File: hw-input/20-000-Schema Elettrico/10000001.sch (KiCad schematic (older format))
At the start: 34 parts, among them P1 PLUG_01X04_254, P2 PLUG_01X04_254, P3 PLUG_01X04_254, P4 PLUG_01X04_254, P5 PLUG_01X04_254, P6 PLUG_01X04_254, P7 PLUG_01X04_254, P8 PLUG_01X04_254, U1 TCA9554, U2 TLP291(SE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

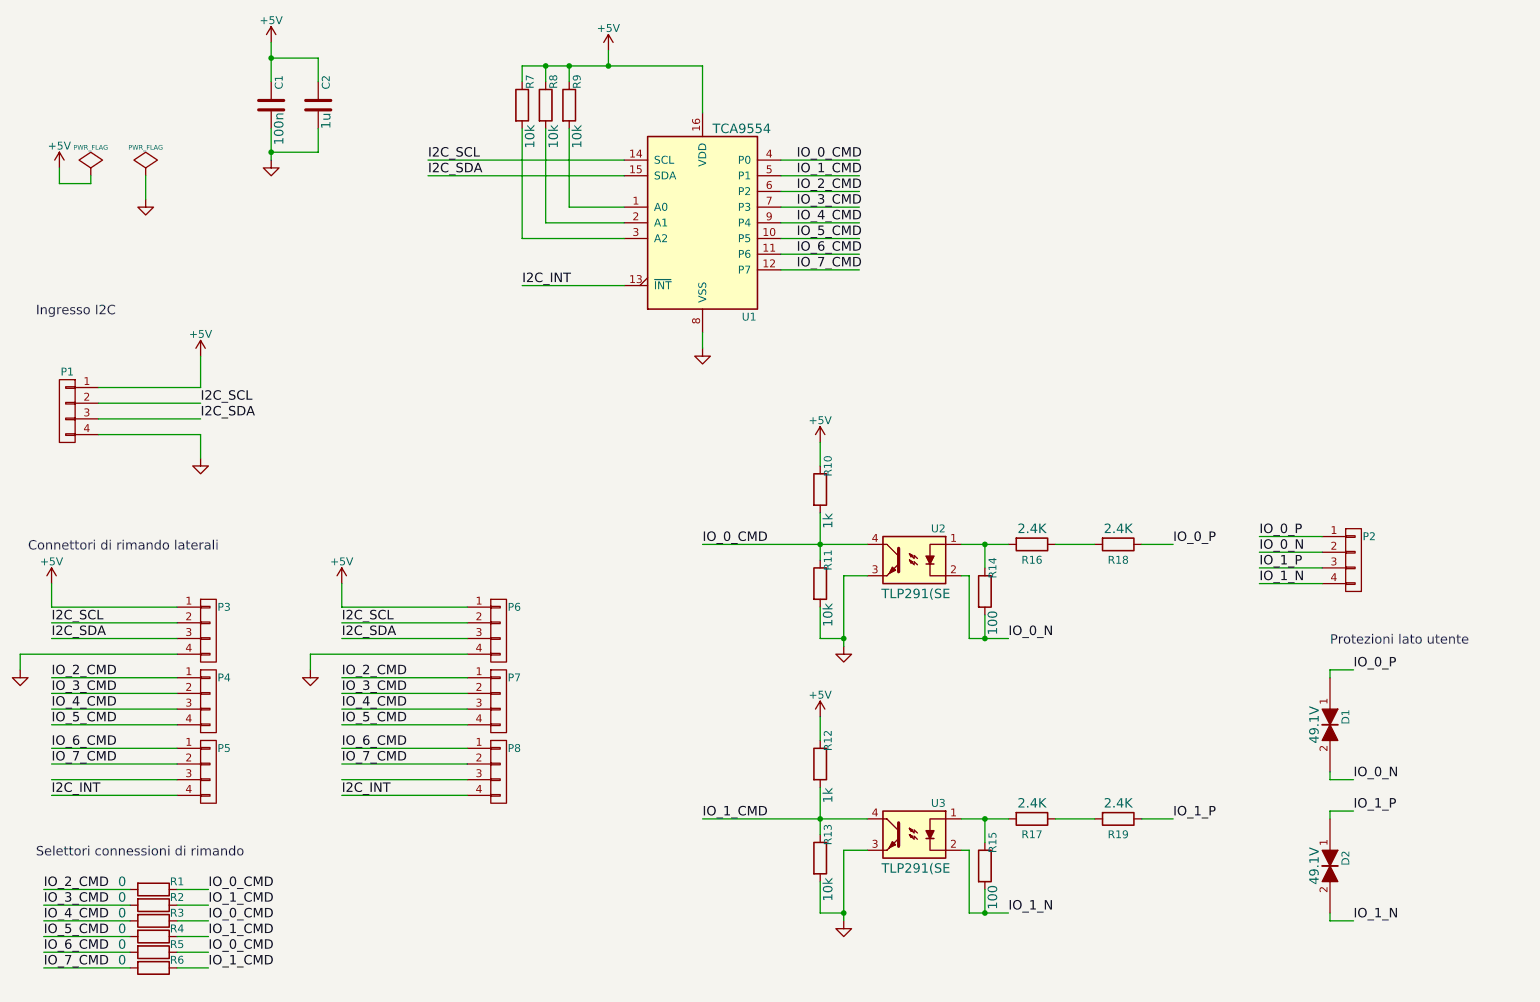
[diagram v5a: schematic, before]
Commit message: completato schema elettrico e sbroglio
Signed-off-by: CrazyDiamond <crazyd14@gmail.com>
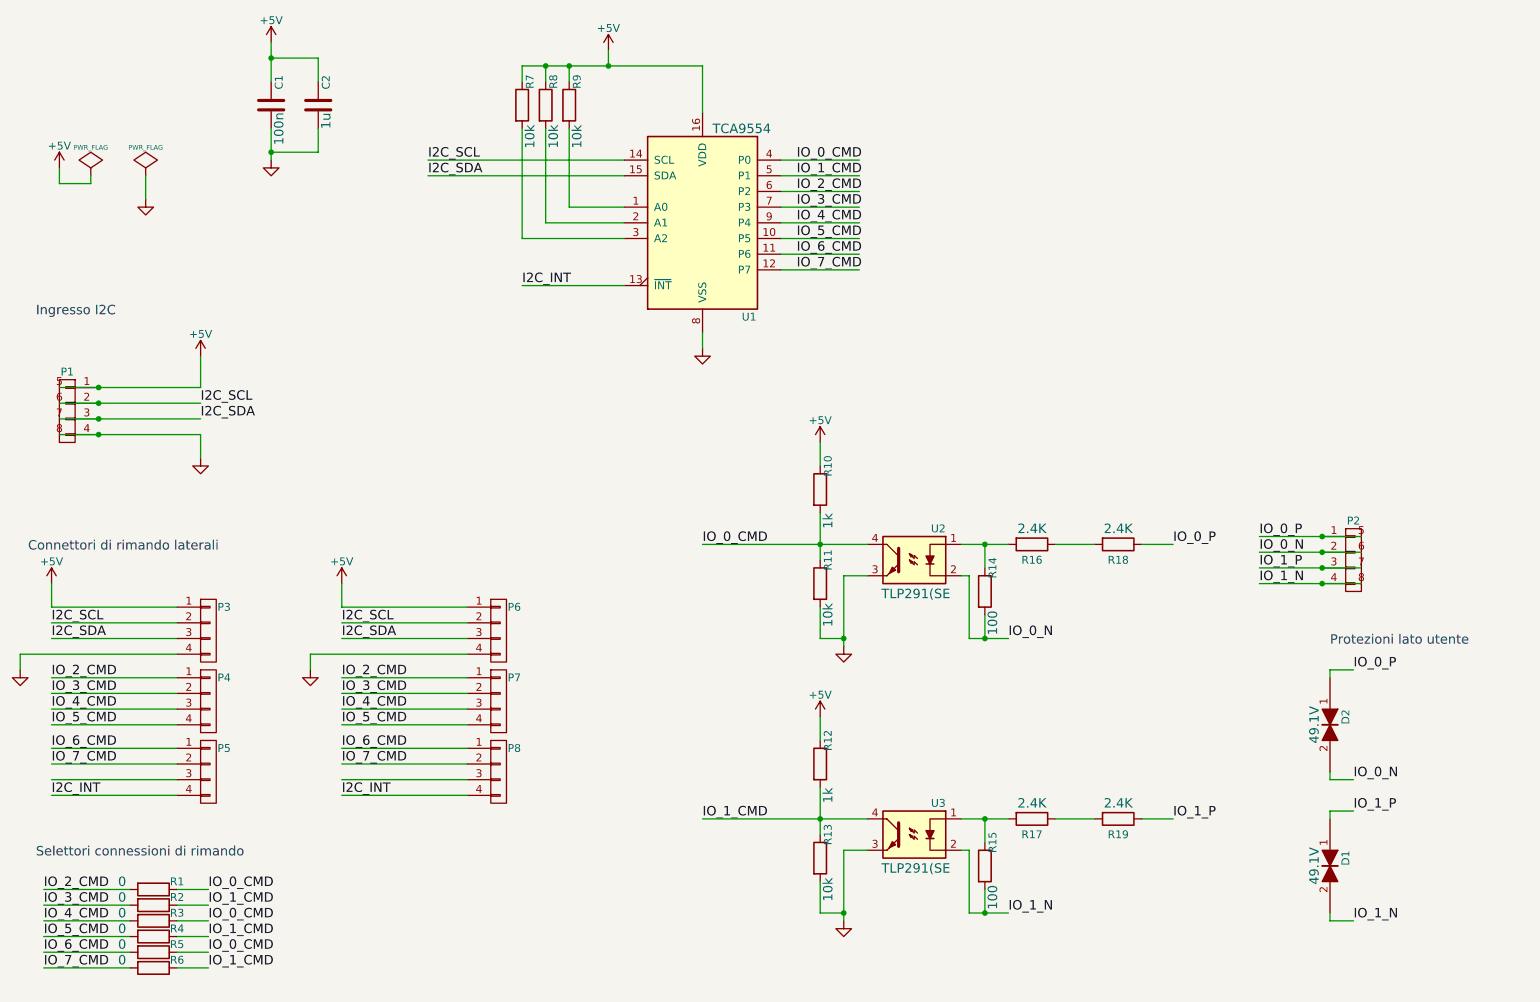
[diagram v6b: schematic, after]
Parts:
- removed P1, P2: PLUG_01X04_254, Socket_Strips:Socket_Strip_Straight_1x04, symbol PLUG_01X04_254
- added P1, P2: TERMINAL_01X04_250_RA_SPRING, os_terminal_block:1770908, symbol TERMINAL_01X04_250_RA_SPRING
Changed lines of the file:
@@
 	1550 1700 1550 1600
 Wire Wire Line
-	1800 3000 2450 3000
+	1550 3000 2450 3000
 Wire Wire Line
 	2450 3000 2450 2800
 Wire Wire Line
-	1800 3300 2450 3300
-Wire Wire Line
-	1800 3100 2450 3100
-Wire Wire Line
-	9600 3950 9200 3950
-Wire Wire Line
-	9600 4050 9200 4050
-Wire Wire Line
-	9600 4150 9200 4150
-Wire Wire Line
-	9600 4250 9200 4250
-Wire Wire Line
-	1800 3200 2450 3200
+	1550 3300 2450 3300
+Wire Wire Line
+	1550 3100 2450 3100
+Wire Wire Line
+	9200 3950 9850 3950
+Wire Wire Line
+	9200 4050 9850 4050
+Wire Wire Line
+	9200 4150 9850 4150
+Wire Wire Line
+	9200 4250 9850 4250
+Wire Wire Line
+	1550 3200 2450 3200
 Wire Wire Line
 	2450 3300 2450 3450
@@
 $EndComp
 $Comp
-L PLUG_01X04_254 P1
-U 1 1 56E8991D
-P 1600 3150
-F 0 "P1" H 1600 3400 50  0000 C CNN
-F 1 "PLUG_01X04_254" H 1700 3150 50  0001 C CNN
-F 2 "Socket_Strips:Socket_Strip_Straight_1x04" H 1500 3300 50  0001 C CNN
-F 3 "" H 1600 3400 50  0000 C CNN
-F 4 "0" H 1700 3500 60  0001 C CNN "NOPOP"
-F 5 "Harwin" H 1800 3600 60  0001 C CNN "MF"
-F 6 "M20-7820446" H 1900 3700 60  0001 C CNN "MF_PN"
-F 7 "M20-7820446" H 2000 3800 60  0001 C CNN "VAL"
-	1    1600 3150
-	-1   0    0    -1
-$EndComp
-$Comp
 L PLUG_01X04_254 P3
 U 1 1 56E89F8C
@@
 $EndComp
 $Comp
-L PLUG_01X04_254 P2
-U 1 1 56E8BD81
-P 9800 4100
-F 0 "P2" H 9900 4250 50  0000 C CNN
-F 1 "PLUG_01X04_254" H 9900 4100 50  0001 C CNN
-F 2 "Socket_Strips:Socket_Strip_Straight_1x04" H 9700 4250 50  0001 C CNN
-F 3 "" H 9800 4350 50  0000 C CNN
-F 4 "0" H 9900 4450 60  0001 C CNN "NOPOP"
-F 5 "Harwin" H 10000 4550 60  0001 C CNN "MF"
-F 6 "M20-7820446" H 10100 4650 60  0001 C CNN "MF_PN"
-F 7 "M20-7820446" H 10200 4750 60  0001 C CNN "VAL"
-	1    9800 4100
-	1    0    0    -1
-$EndComp
-$Comp
 L R_0_0603_5 R1
 U 1 1 56E8C920
@@
 U 1 1 56E8F00D
 P 9650 5150
-F 0 "D1" H 9600 5250 50  0000 C CNN
+F 0 "D2" H 9600 5250 50  0000 C CNN
 F 1 "TVS_SMC_49.1V" H 9650 5000 50  0001 C CNN
 F 2 "Diodes_SMD:SMC_Standard" H 9550 5200 50  0001 C CNN
@@
 U 1 1 56E8F0C7
 P 9650 6050
-F 0 "D2" H 9600 6150 50  0000 C CNN
+F 0 "D1" H 9600 6150 50  0000 C CNN
 F 1 "TVS_SMC_49.1V" H 9650 5900 50  0001 C CNN
 F 2 "Diodes_SMD:SMC_Standard" H 9550 6100 50  0001 C CNN
@@
 	1    0    0    -1
 $EndComp
+$Comp
+L TERMINAL_01X04_250_RA_SPRING P1
+U 1 1 57E1C341
+P 1600 3150
+F 0 "P1" H 1600 3400 50  0000 C CNN
+F 1 "TERMINAL_01X04_250_RA_SPRING" H 1700 3150 50  0001 C CNN
+F 2 "os_terminal_block:1770908" H 1500 3300 50  0001 C CNN
+F 3 "" H 1600 3400 50  0001 C CNN
+F 4 "0" H 1700 3500 60  0001 C CNN "NOPOP"
+F 5 "Phoenix Contact" H 1800 3600 60  0001 C CNN "MF"
+F 6 "1770908" H 1900 3700 60  0001 C CNN "MF_PN"
+F 7 "1770908" H 2000 3800 60  0001 C CNN "VAL"
+	1    1600 3150
+	-1   0    0    -1
+$EndComp
+$Comp
+L TERMINAL_01X04_250_RA_SPRING P2
+U 1 1 57E1CE1B
+P 9800 4100
+F 0 "P2" H 9800 4350 50  0000 C CNN
+F 1 "TERMINAL_01X04_250_RA_SPRING" H 9900 4100 50  0001 C CNN
+F 2 "os_terminal_block:1770908" H 9700 4250 50  0001 C CNN
+F 3 "" H 9800 4350 50  0001 C CNN
+F 4 "0" H 9900 4450 60  0001 C CNN "NOPOP"
+F 5 "Phoenix Contact" H 10000 4550 60  0001 C CNN "MF"
+F 6 "1770908" H 10100 4650 60  0001 C CNN "MF_PN"
+F 7 "1770908" H 10200 4750 60  0001 C CNN "VAL"
+	1    9800 4100
+	1    0    0    -1
+$EndComp
+Connection ~ 1800 3000
+Connection ~ 1800 3100
+Connection ~ 1800 3200
+Connection ~ 1800 3300
+Connection ~ 9600 3950
+Connection ~ 9600 4050
+Connection ~ 9600 4150
+Connection ~ 9600 4250
 $EndSCHEMATC
